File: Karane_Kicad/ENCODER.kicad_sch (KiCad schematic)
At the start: 8 parts, among them U25 AS5145B, U26 AS5145B

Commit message: Agregado Mosfet dual
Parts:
- J12, J13: value ~ -> (none)

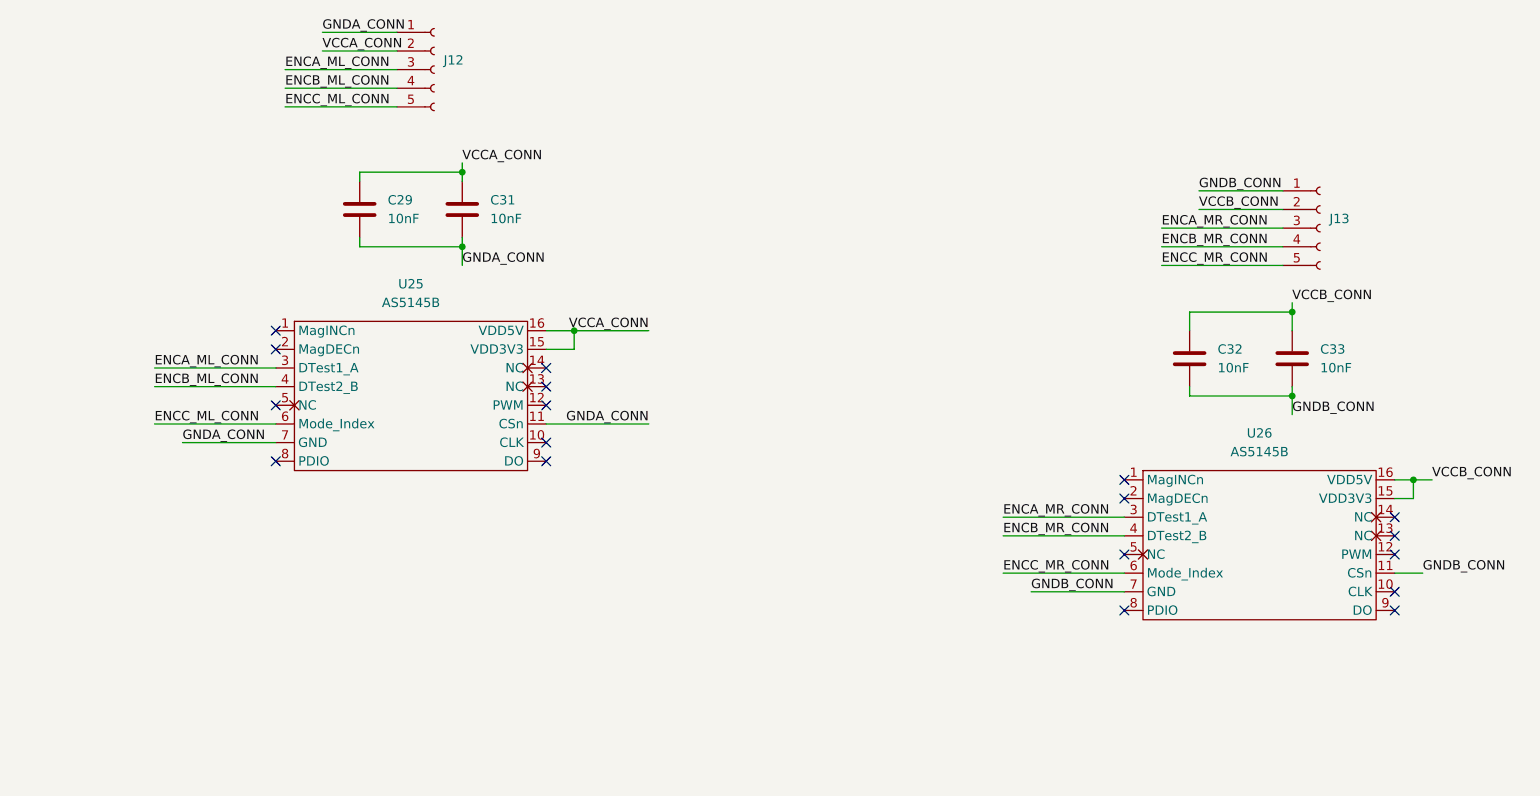
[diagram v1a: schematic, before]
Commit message: Cambio de f103 a f401
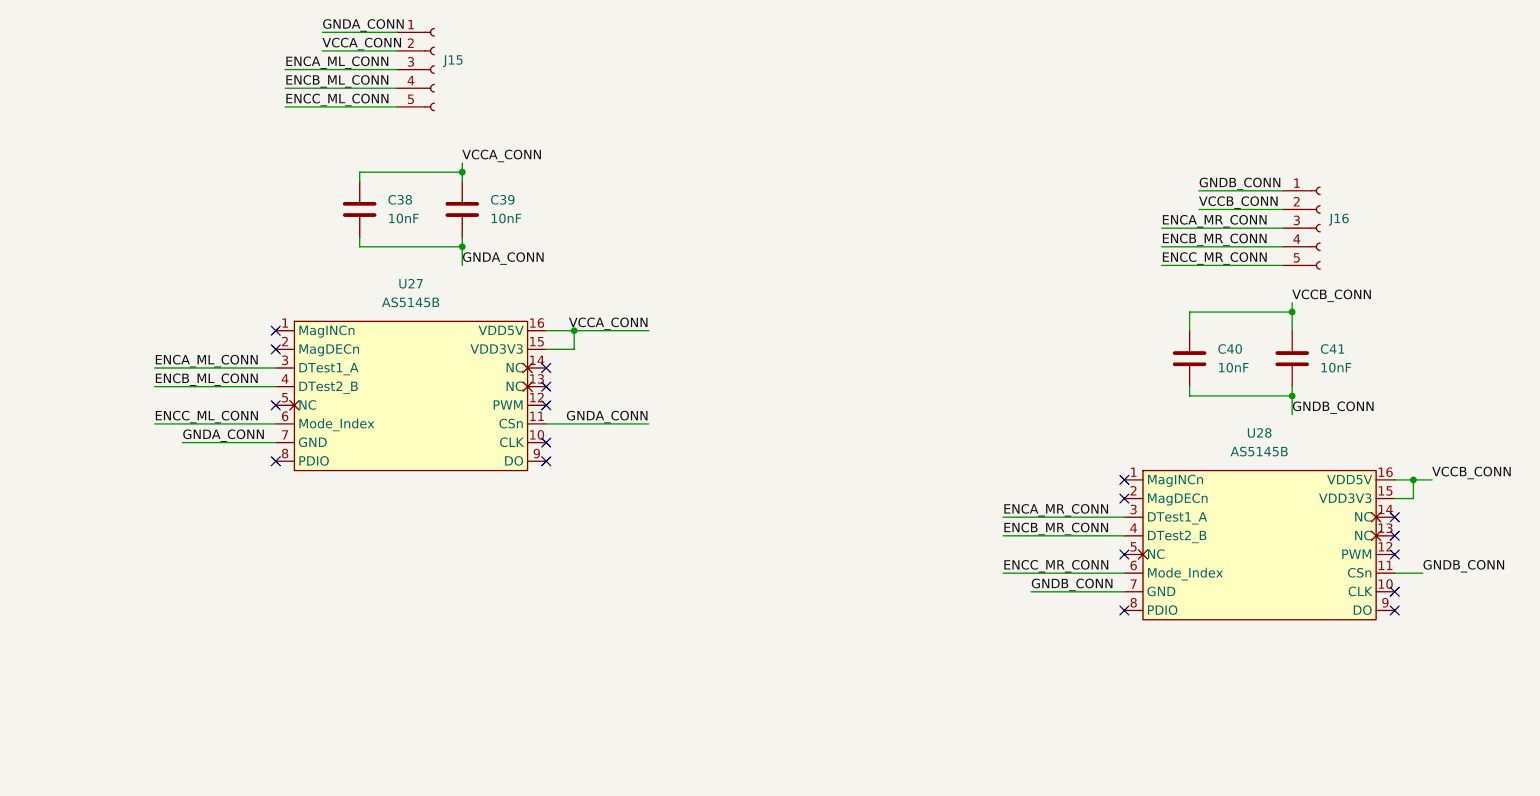
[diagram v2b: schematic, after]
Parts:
- renumbered C29 to C38, C31 to C39, C32 to C40, C33 to C41, J12 to J15, J13 to J16, U25 to U27, U26 to U28
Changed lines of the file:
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@@
 		(in_pos_files yes)
 		(dnp no)
-		(property "Reference" "C31"
+		(property "Reference" "C39"
 			(at 93.98 69.8499 0)
 			(show_name no)
@@
 			(project "Karane_Kicad"
 				(path "/65dfbecc-0fbf-480c-951c-b0d4a210bc14/f114eb8e-0d54-4743-99d0-5b8ba6d5a2a1"
-					(reference "C31")
+					(reference "C39")
 					(unit 1)
 				)
@@
 		(dnp no)
 		(fields_autoplaced yes)
-		(property "Reference" "U25"
+		(property "Reference" "U27"
 			(at 83.185 81.28 0)
 			(show_name no)
@@
 			(project "Karane_Kicad"
 				(path "/65dfbecc-0fbf-480c-951c-b0d4a210bc14/f114eb8e-0d54-4743-99d0-5b8ba6d5a2a1"
-					(reference "U25")
+					(reference "U27")
 					(unit 1)
 				)
@@
 		(dnp no)
 		(fields_autoplaced yes)
-		(property "Reference" "J12"
+		(property "Reference" "J15"
 			(at 87.63 50.7999 0)
 			(show_name no)
@@
 			(project "Karane_Kicad"
 				(path "/65dfbecc-0fbf-480c-951c-b0d4a210bc14/f114eb8e-0d54-4743-99d0-5b8ba6d5a2a1"
-					(reference "J12")
+					(reference "J15")
 					(unit 1)
 				)
@@
 		(in_pos_files yes)
 		(dnp no)
-		(property "Reference" "C29"
+		(property "Reference" "C38"
 			(at 80.01 69.8499 0)
 			(show_name no)
@@
 			(project "Karane_Kicad"
 				(path "/65dfbecc-0fbf-480c-951c-b0d4a210bc14/f114eb8e-0d54-4743-99d0-5b8ba6d5a2a1"
-					(reference "C29")
+					(reference "C38")
 					(unit 1)
 				)
@@
 		(dnp no)
 		(fields_autoplaced yes)
-		(property "Reference" "J13"
+		(property "Reference" "J16"
 			(at 208.28 72.3899 0)
 			(show_name no)
@@
 			(project "Karane_Kicad"
 				(path "/65dfbecc-0fbf-480c-951c-b0d4a210bc14/f114eb8e-0d54-4743-99d0-5b8ba6d5a2a1"
-					(reference "J13")
+					(reference "J16")
 					(unit 1)
 				)
@@
 		(in_pos_files yes)
 		(dnp no)
-		(property "Reference" "C32"
+		(property "Reference" "C40"
 			(at 193.04 90.1699 0)
 			(show_name no)
@@
 			(project "Karane_Kicad"
 				(path "/65dfbecc-0fbf-480c-951c-b0d4a210bc14/f114eb8e-0d54-4743-99d0-5b8ba6d5a2a1"
-					(reference "C32")
+					(reference "C40")
 					(unit 1)
 				)
@@
 		(in_pos_files yes)
 		(dnp no)
-		(property "Reference" "C33"
+		(property "Reference" "C41"
 			(at 207.01 90.1699 0)
 			(show_name no)
@@
 			(project "Karane_Kicad"
 				(path "/65dfbecc-0fbf-480c-951c-b0d4a210bc14/f114eb8e-0d54-4743-99d0-5b8ba6d5a2a1"
-					(reference "C33")
+					(reference "C41")
 					(unit 1)
 				)
@@
 		(dnp no)
 		(fields_autoplaced yes)
-		(property "Reference" "U26"
+		(property "Reference" "U28"
 			(at 198.755 101.6 0)
 			(show_name no)
@@
 			(project "Karane_Kicad"
 				(path "/65dfbecc-0fbf-480c-951c-b0d4a210bc14/f114eb8e-0d54-4743-99d0-5b8ba6d5a2a1"
-					(reference "U26")
-					(unit 1)
-				)
+					(reference "U28")
+					(unit 1)
+				)

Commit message: finalizado pcb v2
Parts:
- removed C38, C40: 10nF, Capacitor_SMD:C_0603_1608Metric_Pad1.08x0.95mm_HandSolder, symbol Device:C
- removed U27, U28: AS5145B, Package_SO:SSOP-16_5.3x6.2mm_P0.65mm, symbol Micromouse_Library:AS5145B
- added JP1, JP2: Jumper_2_Open, Jumper:SolderJumper-2_P1.3mm_Open_RoundedPad1.0x1.5mm, symbol Jumper:Jumper_2_Open
- added R61, R62: 10k, Resistor_SMD:R_0603_1608Metric_Pad0.98x0.95mm_HandSolder, symbol Device:R
- added U27, U28: MT6701CT, Package_SO:SO-8_3.9x4.9mm_P1.27mm, symbol Sensor_Magnetic:MT6701CT
- C39, C41: value 10nF -> 100nF
- J15, J16: footprint Footprint:as5145_mod_1.27 -> Footprint:AS5145_Mod
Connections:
- net ENCA_ML_CONN: now also U27.6 (A)
- net ENCA_MR_CONN: now also U28.6 (A)
- net ENCB_ML_CONN: now also U27.7 (B)
- net ENCB_MR_CONN: now also U28.7 (B)
- net ENCC_ML_CONN: now also U27.8 (Z)
- net ENCC_MR_CONN: now also U28.8 (Z)
- net GNDA_CONN: now also R61.2, U27.4 (GND)
- net GNDB_CONN: now also R62.2, U28.4 (GND)
- net VCCA_CONN: now also JP1.1 (A), U27.1 (VDD)
- net VCCB_CONN: now also JP2.1 (A), U28.1 (VDD)
- new net: JP1.2 (B), R61.1, U27.2 (MODE)
- new net: JP2.2 (B), R62.1, U28.2 (MODE)
- no-connect marks 18 -> 4
